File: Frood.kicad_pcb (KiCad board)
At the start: 2 copper layers, 17.8 x 33.9 mm, 42 parts, among them J1 Conn_02x13+5, SW1 RESET, SW2 BOOT, U1 RP2040, U2 ZD25WQ16BUIGR, U3 SPX3819M5-L-3-3/TR, Y1 TXM12M0004252LBCEO00T

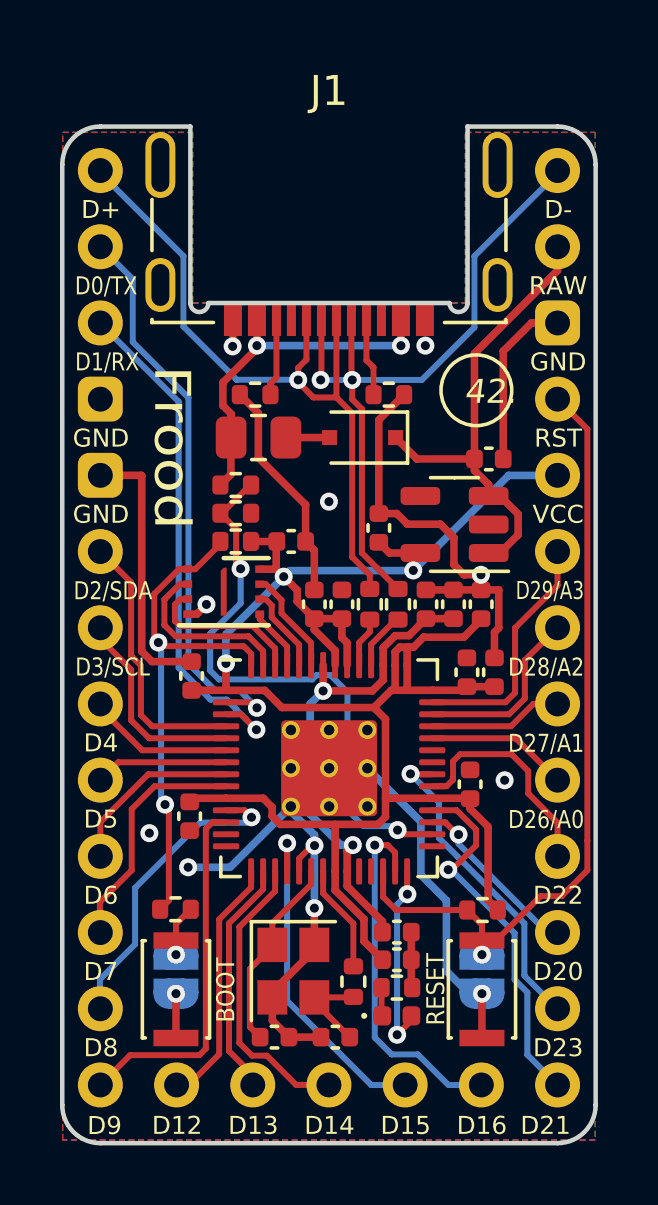
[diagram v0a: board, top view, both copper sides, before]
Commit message: Rev6 update
* Use a 4 MB (32 Mb) flash chip instead
* Minor routing fine-tuning
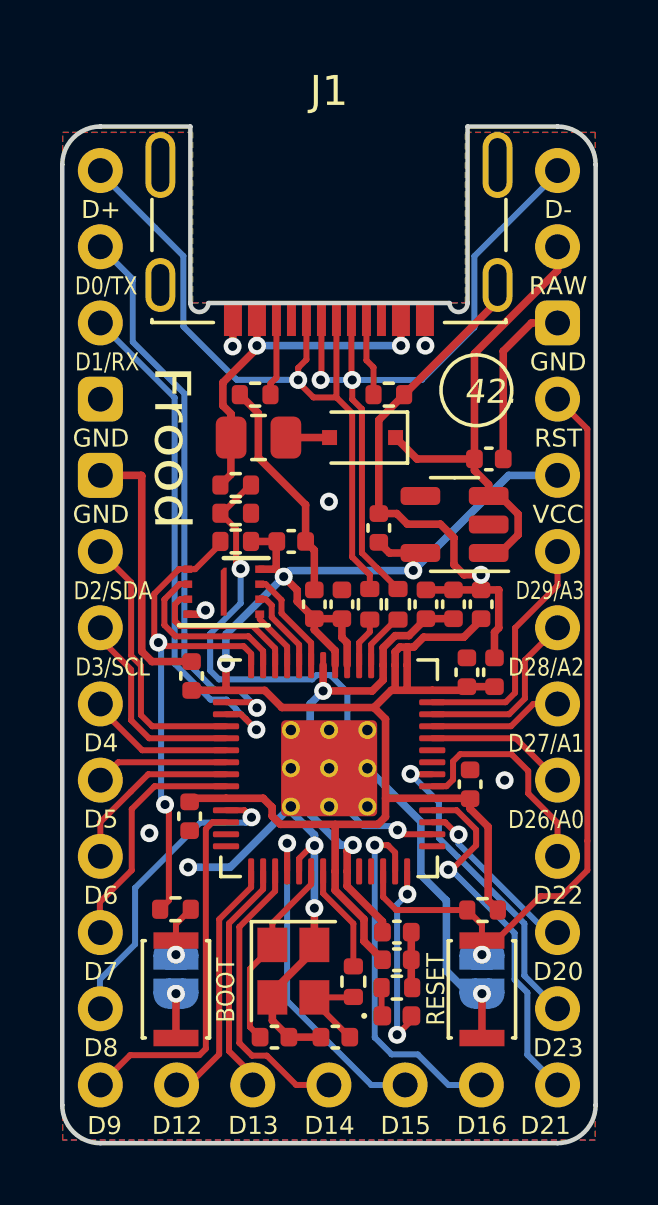
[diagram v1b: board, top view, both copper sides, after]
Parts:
- U2: value ZD25WQ16BUIGR -> P25Q32H-UXH-IR
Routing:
- net GND: track 67.3 -> 72.1 mm
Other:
- board text added: "Frood rev6 42keebs.eu 2022"
- board text removed: "Frood rev5 42keebs.eu 2022"

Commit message: Rev7 update
* Use a Winbond 4 MB flash chip
* Use higher quality Panasonic reset/boot switches
* A few routing tweaks
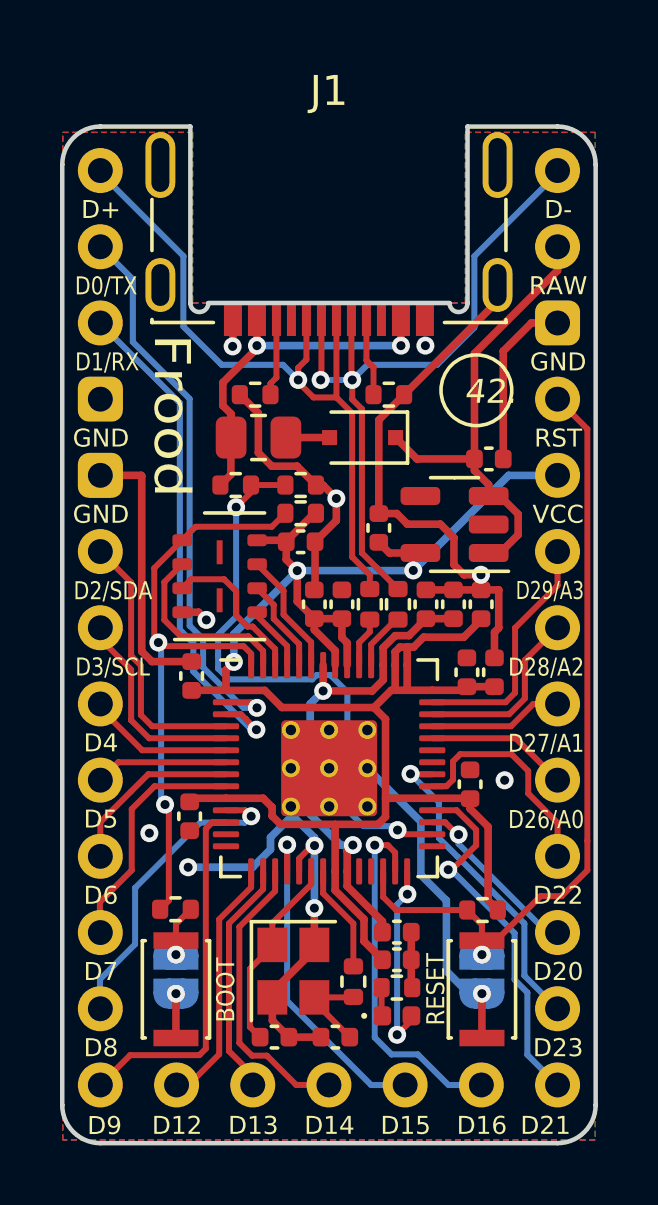
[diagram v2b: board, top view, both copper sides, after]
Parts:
- U2: value P25Q32H-UXH-IR -> W25Q32JVUUIQ; footprint 42keebs:DFN-8-1EP_3x2mm_P0.5mm_EP0.2x1.6mm -> 42keebs:USON-8_4x3mm_P0.8mm
- moved R12 2.36 mm to (125.4, 66.7)
- moved R7 2.36 mm to (125.4, 67.7)
- moved U2 0.53 mm to (122.7, 69.8)
- moved C5 0.31 mm to (125.4, 68.6)
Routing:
- net /QSPI_SS: track 17.4 -> 20.4 mm
- net GND: track 72.1 -> 74.1 mm
- net +3V3: track 66.0 -> 66.7 mm
- net /QSPI_SD3: track 3.53 -> 4.11 mm
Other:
- board text added: "Frood rev7 42keebs.eu 2023"
- board text removed: "Frood rev6 42keebs.eu 2022"

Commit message: Rev8 update
* Add a 2-way solder jumper to select VBUS OUT or VBUS IN on the RAW pin
* Use orange indicator LED again
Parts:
- added JP3: VBUS_SEL, 42keebs:SolderJumper-3_P1.3mm_Bridged12_RoundedPad0.8x1mm, B.Cu at (131.9, 63.3)
- moved C1 1.67 mm to (130.0, 65.9), turned to 180 degrees
- moved C15 0.07 mm to (121.7, 77.8)
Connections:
- net Net-(R11-Pad1) renamed /VSENSE
- C1 pad 1: /RAW -> /VBUS_OUT
- D1 pad 1: /RAW -> /VBUS_OUT
- U3 pad 1: /RAW -> /VBUS_OUT
- U3 pad 3: /RAW -> /VBUS_OUT
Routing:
- net GND: track 74.1 -> 58.9 mm
- net /RAW: track 15.7 -> 5.70 mm
- net /VBUS_OUT: track 0.00 -> 9.79 mm, vias 0 -> 1
- net VBUS: track 12.6 -> 17.4 mm, vias 2 -> 3
- net /VSENSE: track 19.6 -> 16.2 mm
- net /QSPI_SS: track 20.4 -> 22.9 mm
- net /~{RESET}: track 26.1 -> 25.4 mm, vias 1 -> 2
- net +3V3: track 66.7 -> 67.4 mm, vias 3 -> 4
- net /D9: track 12.1 -> 12.7 mm
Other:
- board text added: "Frood rev8 42keebs.eu 2023"
- board text removed: "Frood rev7 42keebs.eu 2023"

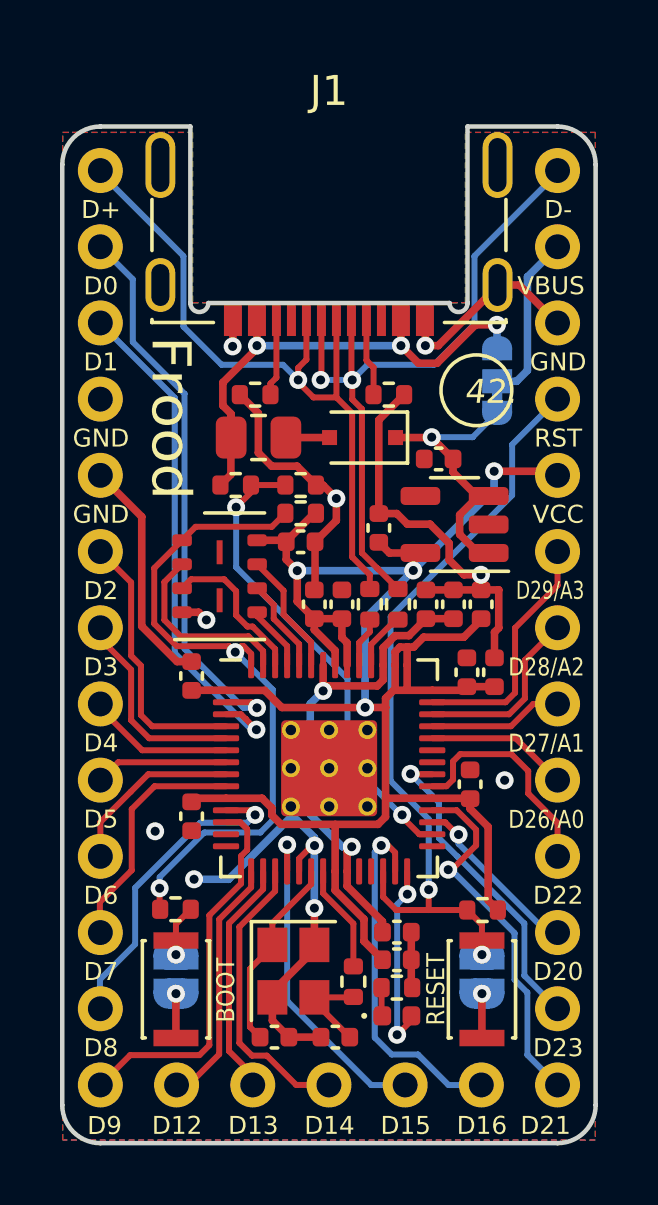
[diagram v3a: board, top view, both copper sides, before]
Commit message: Rev9 update
* Allows converting left-hand side GND pins into GPIO10,11 pins
* Drop VBUS IN/OUT solder jumper, RAW pin now connected between the Schottky and fuse/regulator
* Uses a different (but equivalent) USB-C socket
* Routing and silkscreen tweaks/improvements
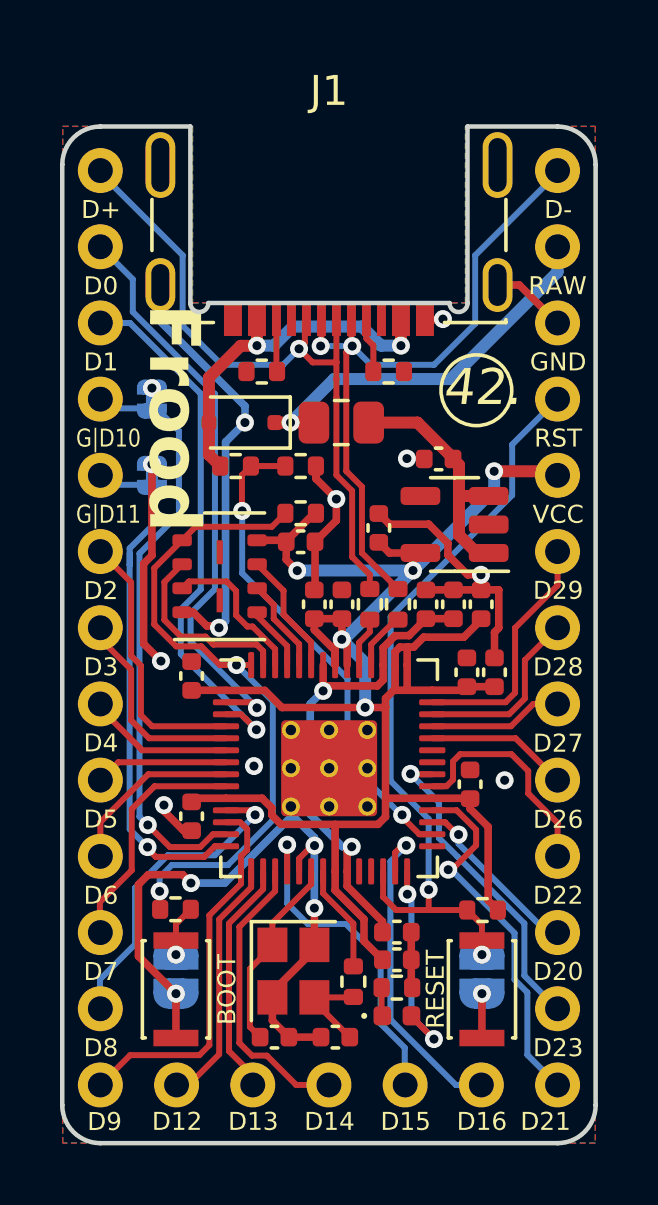
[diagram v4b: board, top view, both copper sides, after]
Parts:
- added JP4: Jumper_2_Bridged, 42keebs:SolderJumper-2_P0.8mm_Bridged_RoundedPad0.5x1mm, B.Cu at (120.4, 66.4)
- J1: footprint 42keebs:PinHeader_2x13+5_P2.54mm_Vertical_Elite-C -> 42keebs:PinHeader_2x13+5_P2.54mm_Vertical_Frood
- JP3: value VBUS_SEL -> Jumper_2_Bridged; footprint 42keebs:SolderJumper-3_P1.3mm_Bridged12_RoundedPad0.8x1mm -> 42keebs:SolderJumper-2_P0.8mm_Bridged_RoundedPad0.5x1mm
- SW1, SW2: footprint Button_Switch_SMD:SW_SPST_CK_KXT3 -> 42keebs:SW_SPST_CK_KXT3
- USB1: footprint 42keebs:Molex-216990_GCT-USB45xx_HRO-TYPE-C-31-M-13x-PiMicro -> 42keebs:Molex-216990_GCT-USB45xx_HRO-TYPE-C-31-M-13x-Frood
- moved JP3 11.5 mm to (120.4, 63.9)
- moved D1 4.05 mm to (123.4, 64.7)
- moved USB1 3.70 mm to (126.3, 58.6)
- moved F1 2.80 mm to (126.7, 64.7)
- moved R2 0.80 mm to (124.1, 63.0)
- moved R1 0.77 mm to (128.3, 63.0)
- moved R11 0.63 mm to (123.2, 66.1)
- moved R12 0.63 mm to (125.4, 66.1)
- moved LOGO1 0.21 mm to (126.3, 67.5)
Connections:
- C1 pad 1: /VBUS_OUT -> /VIN
- D1 pad 1: /VBUS_OUT -> /RAW
- D1 pad 2: Net-(D1-Pad2) -> VBUS
- F1 pad 1: VBUS -> /RAW
- F1 pad 2: Net-(D1-Pad2) -> /VIN
- J1 pad 4: GND -> /GND/D10
- J1 pad 5: GND -> /GND/D11
- JP3 pad 1: /VBUS_OUT -> /GND/D10
- JP3 pad 2: /RAW -> GND
- U1 pad 13: unconnected-(U1-Pad13) -> /GND/D10
- U1 pad 14: unconnected-(U1-Pad14) -> /GND/D11
- U3 pad 1: /VBUS_OUT -> /VIN
- U3 pad 3: /VBUS_OUT -> /VIN
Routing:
- net /GND/D10: track 0.00 -> 19.9 mm, vias 0 -> 1
- net /GND/D11: track 0.00 -> 17.8 mm, vias 0 -> 1
- net /VBUS_OUT: track 9.79 -> 0.00 mm, vias 1 -> 0
- net /VIN: track 0.00 -> 8.18 mm
- net GND: track 58.9 -> 66.4 mm, vias 12 -> 17
- net /RAW: track 5.70 -> 13.1 mm, vias 0 -> 1
- net VBUS: track 17.4 -> 12.2 mm, vias 3 -> 2
- net Net-(D1-Pad2): track 1.46 -> 0.00 mm
- net /D+: track 24.0 -> 22.9 mm
- net /D1/RX: track 17.0 -> 18.1 mm
- net /D-: track 23.8 -> 22.9 mm
- net Net-(USB1-CC2): track 2.58 -> 1.73 mm
- net /D16: track 11.9 -> 11.0 mm
- net /QSPI_SS: track 22.9 -> 22.1 mm
- net Net-(USB1-CC1): track 2.59 -> 1.82 mm
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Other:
- board text added: "Frood rev9 42keebs.eu 2024"
- board text removed: "Frood rev8 42keebs.eu 2023"
